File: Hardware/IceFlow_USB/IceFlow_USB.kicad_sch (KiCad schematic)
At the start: 23 parts, among them J1 Barrel_Jack_Switch, J2 Conn_01x04, J3 TFT_Display_wTouch, J4 Conn_02x02_Odd_Even, J5 USB_MICRO-B_SMT, J6 Conn_02x05_Odd_Even, J8 Power_Sw, U1 NCP1117-3.3_SOT223, U2 ESP32-WROVER-E

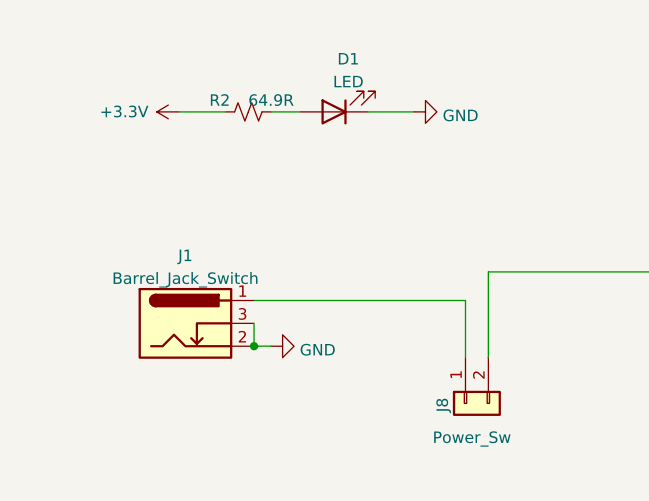
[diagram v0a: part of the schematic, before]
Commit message: Added second PCB with USB Power.
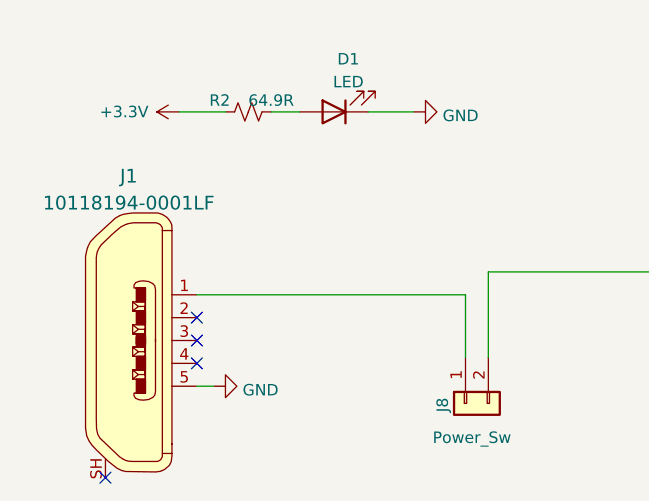
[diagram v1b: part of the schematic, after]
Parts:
- removed J1: Barrel_Jack_Switch, Kitecraft_Barrel_Jacks:BarrelJack_Wuerth_6941xx301002, symbol Connector:Barrel_Jack_Switch
- added J1: 10118194-0001LF, Kitecraft_Barrel_Jacks:USB_Micro_B_Female_10118194-0001LF, symbol dk_USB-DVI-HDMI-Connectors:10118194-0001LF
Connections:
- net GND: now also J1.5
- net at J8.1 (Pin_1): now also J1.1
- no-connect marks 12 -> 16
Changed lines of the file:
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@@
   (junction (at 133.35 161.925) (diameter 0) (color 0 0 0 0)
-  )
-  (junction (at 38.1 170.18) (diameter 0) (color 0 0 0 0)
   )
   (no_connect (at 130.81 103.505))
@@
   (no_connect (at 60.96 89.535))
   (no_connect (at 60.96 86.995))
-  (wire (pts (xy 61.595 165.1) (xy 61.595 171.45))
+  (no_connect (at 31.75 172.085))
+  (no_connect (at 31.75 169.545))
+  (no_connect (at 21.59 184.785))
+  (no_connect (at 31.75 167.005))
+  (wire (pts (xy 61.595 164.465) (xy 61.595 171.45))
     (stroke (width 0) (type default) (color 0 0 0 0))
   )
@@
     (stroke (width 0) (type default) (color 0 0 0 0))
   )
-  (wire (pts (xy 38.1 165.1) (xy 61.595 165.1))
+  (wire (pts (xy 31.75 164.465) (xy 61.595 164.465))
     (stroke (width 0) (type default) (color 0 0 0 0))
   )
@@
     (stroke (width 0) (type default) (color 0 0 0 0))
   )
-  (wire (pts (xy 38.1 170.18) (xy 40.005 170.18))
+  (wire (pts (xy 31.75 174.625) (xy 33.655 174.625))
     (stroke (width 0) (type default) (color 0 0 0 0))
   )
@@
     (stroke (width 0) (type default) (color 0 0 0 0))
   )
-  (wire (pts (xy 38.1 167.64) (xy 38.1 170.18))
-    (stroke (width 0) (type default) (color 0 0 0 0))
-  )
   (wire (pts (xy 52.705 53.975) (xy 60.96 53.975))
     (stroke (width 0) (type default) (color 0 0 0 0))
@@
     )
     (pin "1")
-  )
-  (symbol (lib_id "Connector:Barrel_Jack_Switch") (at 30.48 167.64 0) (unit 1)
-    (in_bom yes) (on_board yes) (fields_autoplaced)
-    (property "Reference" "J1" (id 0) (at 30.48 160.1302 0))
-    (property "Value" "Barrel_Jack_Switch" (id 1) (at 30.48 162.6671 0))
-    (property "Footprint" "Kitecraft_Barrel_Jacks:BarrelJack_Wuerth_6941xx301002" (id 2) (at 31.75 168.656 0)
-      (effects (font (size 1.27 1.27)) hide)
-    )
-    (property "Datasheet" "~" (id 3) (at 31.75 168.656 0)
-      (effects (font (size 1.27 1.27)) hide)
-    )
-    (pin "1")
-    (pin "2")
-    (pin "3")
   )
   (symbol (lib_id "power:GND") (at 30.48 42.545 270) (unit 1)
@@
     (pin "9")
   )
+  (symbol (lib_id "dk_USB-DVI-HDMI-Connectors:10118194-0001LF") (at 24.13 169.545 0) (unit 1)
+    (in_bom yes) (on_board yes) (fields_autoplaced)
+    (property "Reference" "J1" (id 0) (at 24.1808 151.2877 0)
+      (effects (font (size 1.524 1.524)))
+    )
+    (property "Value" "10118194-0001LF" (id 1) (at 24.1808 154.2811 0)
+      (effects (font (size 1.524 1.524)))
+    )
+    (property "Footprint" "Kitecraft_Barrel_Jacks:USB_Micro_B_Female_10118194-0001LF" (id 2) (at 29.21 164.465 0)
+      (effects (font (size 1.524 1.524)) (justify left) hide)
+    )
+    (property "Datasheet" "http://www.amphenol-icc.com/media/wysiwyg/files/drawing/10118194.pdf" (id 3) (at 29.21 161.925 0)
+      (effects (font (size 1.524 1.524)) (justify left) hide)
+    )
+    (property "Digi-Key_PN" "609-4618-1-ND" (id 4) (at 29.21 159.385 0)
+      (effects (font (size 1.524 1.524)) (justify left) hide)
+    )
+    (property "MPN" "10118194-0001LF" (id 5) (at 29.21 156.845 0)
+      (effects (font (size 1.524 1.524)) (justify left) hide)
+    )
+    (property "Category" "Connectors, Interconnects" (id 6) (at 29.21 154.305 0)
+      (effects (font (size 1.524 1.524)) (justify left) hide)
+    )
+    (property "Family" "USB, DVI, HDMI Connectors" (id 7) (at 29.21 151.765 0)
+      (effects (font (size 1.524 1.524)) (justify left) hide)
+    )
+    (property "DK_Datasheet_Link" "http://www.amphenol-icc.com/media/wysiwyg/files/drawing/10118194.pdf" (id 8) (at 29.21 149.225 0)
+      (effects (font (size 1.524 1.524)) (justify left) hide)
+    )
+    (property "DK_Detail_Page" "/product-detail/en/amphenol-icc-fci/10118194-0001LF/609-4618-1-ND/2785382" (id 9) (at 29.21 146.685 0)
+      (effects (font (size 1.524 1.524)) (justify left) hide)
+    )
+    (property "Description" "CONN RCPT USB2.0 MICRO B SMD R/A" (id 10) (at 29.21 144.145 0)
+      (effects (font (size 1.524 1.524)) (justify left) hide)
+    )
+    (property "Manufacturer" "Amphenol ICC (FCI)" (id 11) (at 29.21 141.605 0)
+      (effects (font (size 1.524 1.524)) (justify left) hide)
+    )
+    (property "Status" "Active" (id 12) (at 29.21 139.065 0)
+      (effects (font (size 1.524 1.524)) (justify left) hide)
+    )
+    (pin "1")
+    (pin "2")
+    (pin "3")
+    (pin "4")
+    (pin "5")
+    (pin "SH")
+  )
   (symbol (lib_id "power:GND") (at 189.23 20.32 270) (unit 1)
     (in_bom yes) (on_board yes)
@@
     (pin "1")
   )
-  (symbol (lib_id "power:GND") (at 40.005 170.18 90) (unit 1)
-    (in_bom yes) (on_board yes) (fields_autoplaced)
-    (property "Reference" "#PWR0102" (id 0) (at 46.355 170.18 0)
-      (effects (font (size 1.27 1.27)) hide)
-    )
-    (property "Value" "GND" (id 1) (at 43.18 170.6138 90)
+  (symbol (lib_id "power:GND") (at 33.655 174.625 90) (unit 1)
+    (in_bom yes) (on_board yes) (fields_autoplaced)
+    (property "Reference" "#PWR0102" (id 0) (at 40.005 174.625 0)
+      (effects (font (size 1.27 1.27)) hide)
+    )
+    (property "Value" "GND" (id 1) (at 36.83 175.0588 90)
       (effects (font (size 1.27 1.27)) (justify right))
     )
-    (property "Footprint" "" (id 2) (at 40.005 170.18 0)
-      (effects (font (size 1.27 1.27)) hide)
-    )
-    (property "Datasheet" "" (id 3) (at 40.005 170.18 0)
+    (property "Footprint" "" (id 2) (at 33.655 174.625 0)
+      (effects (font (size 1.27 1.27)) hide)
+    )
+    (property "Datasheet" "" (id 3) (at 33.655 174.625 0)
       (effects (font (size 1.27 1.27)) hide)
     )
@@
       (reference "H4") (unit 1) (value "MountingHole") (footprint "MountingHole:MountingHole_3.2mm_M3_DIN965")
     )
-    (path "/1e4a1739-fbcb-4101-8bb4-4a741cb898fb"
-      (reference "J1") (unit 1) (value "Barrel_Jack_Switch") (footprint "Kitecraft_Barrel_Jacks:BarrelJack_Wuerth_6941xx301002")
+    (path "/64a8a42b-bf18-45c7-9c5e-7b2960ac0924"
+      (reference "J1") (unit 1) (value "10118194-0001LF") (footprint "Kitecraft_Barrel_Jacks:USB_Micro_B_Female_10118194-0001LF")
     )
     (path "/352a5e21-245a-453c-8c8e-43ae95e0e8cd"

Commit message: Pin map changes
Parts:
- D1: footprint LED_SMD:LED_0805_2012Metric_Pad1.15x1.40mm_HandSolder -> LED_SMD:LED_1206_3216Metric_Pad1.42x1.75mm_HandSolder
- R2: footprint Resistor_SMD:R_0805_2012Metric_Pad1.20x1.40mm_HandSolder -> Resistor_SMD:R_1206_3216Metric_Pad1.30x1.75mm_HandSolder
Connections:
- net TPA_CS: now also J6.3 (Pin_3), U2.11 (DAC_2/ADC2_CH9/GPIO26); no longer J6.4 (Pin_4), U2.24 (ADC2_CH2/GPIO2)
- net TPB_CS: now also J6.4 (Pin_4), U2.24 (ADC2_CH2/GPIO2); no longer J6.3 (Pin_3), U2.11 (DAC_2/ADC2_CH9/GPIO26)
- net TFT_CS renamed TOUCH_CS
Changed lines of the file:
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@@
     (stroke (width 0) (type default) (color 0 0 0 0))
   )
-  (label "TPB_CS" (at 132.08 70.485 0)
+  (label "TPB_CS" (at 132.08 42.545 0)
     (effects (font (size 1.27 1.27)) (justify left bottom))
   )
@@
     (effects (font (size 1.27 1.27)) (justify left bottom))
   )
-  (label "TFT_CS" (at 189.23 43.18 0)
+  (label "TOUCH_CS" (at 189.23 43.18 0)
     (effects (font (size 1.27 1.27)) (justify left bottom))
   )
@@
     (effects (font (size 1.27 1.27)) (justify left bottom))
   )
-  (label "TPA_CS" (at 182.245 107.95 0)
+  (label "TPA_CS" (at 202.565 107.95 0)
     (effects (font (size 1.27 1.27)) (justify left bottom))
   )
@@
     (effects (font (size 1.27 1.27)) (justify left bottom))
   )
-  (label "TFT_CS" (at 132.08 60.325 0)
+  (label "TOUCH_CS" (at 132.08 60.325 0)
     (effects (font (size 1.27 1.27)) (justify left bottom))
   )
@@
     (effects (font (size 1.27 1.27)) (justify left bottom))
   )
-  (label "TPA_CS" (at 132.08 42.545 0)
+  (label "TPA_CS" (at 132.08 70.485 0)
     (effects (font (size 1.27 1.27)) (justify left bottom))
   )
@@
     (effects (font (size 1.27 1.27)) (justify left bottom))
   )
-  (label "TPB_CS" (at 201.295 107.95 0)
+  (label "TPB_CS" (at 182.245 107.95 0)
     (effects (font (size 1.27 1.27)) (justify left bottom))
   )
@@
     (property "Reference" "D1" (id 0) (at 48.5775 138.2862 0))
     (property "Value" "LED" (id 1) (at 48.5775 140.8231 0))
-    (property "Footprint" "LED_SMD:LED_0805_2012Metric_Pad1.15x1.40mm_HandSolder" (id 2) (at 46.99 144.145 0)
+    (property "Footprint" "LED_SMD:LED_1206_3216Metric_Pad1.42x1.75mm_HandSolder" (id 2) (at 46.99 144.145 0)
       (effects (font (size 1.27 1.27)) hide)
     )
@@
     (property "Reference" "R2" (id 0) (at 34.29 142.875 90))
     (property "Value" "64.9R" (id 1) (at 40.005 142.875 90))
-    (property "Footprint" "Resistor_SMD:R_0805_2012Metric_Pad1.20x1.40mm_HandSolder" (id 2) (at 37.465 144.145 0)
+    (property "Footprint" "Resistor_SMD:R_1206_3216Metric_Pad1.30x1.75mm_HandSolder" (id 2) (at 37.465 144.145 0)
       (effects (font (size 1.27 1.27)) hide)
     )
@@
     )
     (path "/2460d235-2c76-4e55-b43b-69ba996c31c9"
-      (reference "D1") (unit 1) (value "LED") (footprint "LED_SMD:LED_0805_2012Metric_Pad1.15x1.40mm_HandSolder")
+      (reference "D1") (unit 1) (value "LED") (footprint "LED_SMD:LED_1206_3216Metric_Pad1.42x1.75mm_HandSolder")
     )
     (path "/b06ecf3c-0e3f-4017-bb6d-0a3c37b098e1"
@@
     )
     (path "/571b50bb-72aa-441a-a0e3-b564c0d0e486"
-      (reference "R2") (unit 1) (value "64.9R") (footprint "Resistor_SMD:R_0805_2012Metric_Pad1.20x1.40mm_HandSolder")
+      (reference "R2") (unit 1) (value "64.9R") (footprint "Resistor_SMD:R_1206_3216Metric_Pad1.30x1.75mm_HandSolder")
     )
     (path "/a2d00796-078f-401b-983d-8b8112e5c730"
